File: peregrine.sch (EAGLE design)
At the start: 67 parts, among them IC2 LMV358IDGKR, J1 USB MICRO, U1 ITG-3200, U2 ADXL345, U4 3.3V, U5 ATMEGA32U4-XUAU, Y1 16MHz KX-7

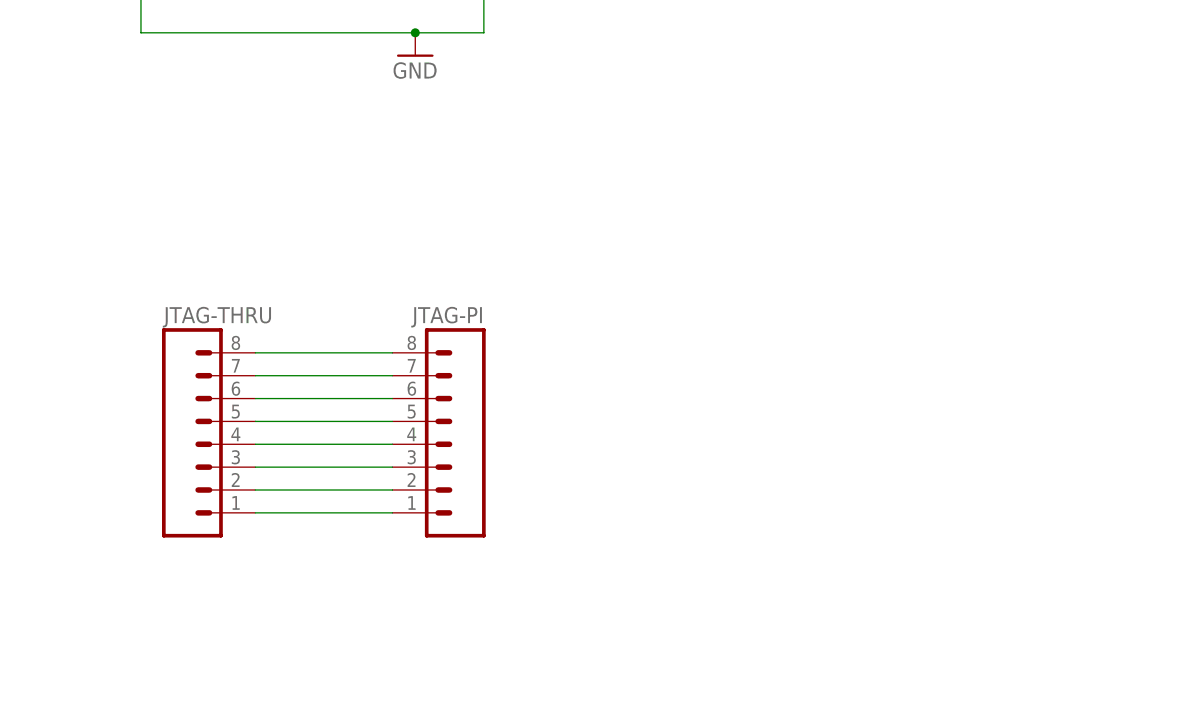
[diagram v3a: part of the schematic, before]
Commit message: Added outline and Pi GPIO, crappy placement
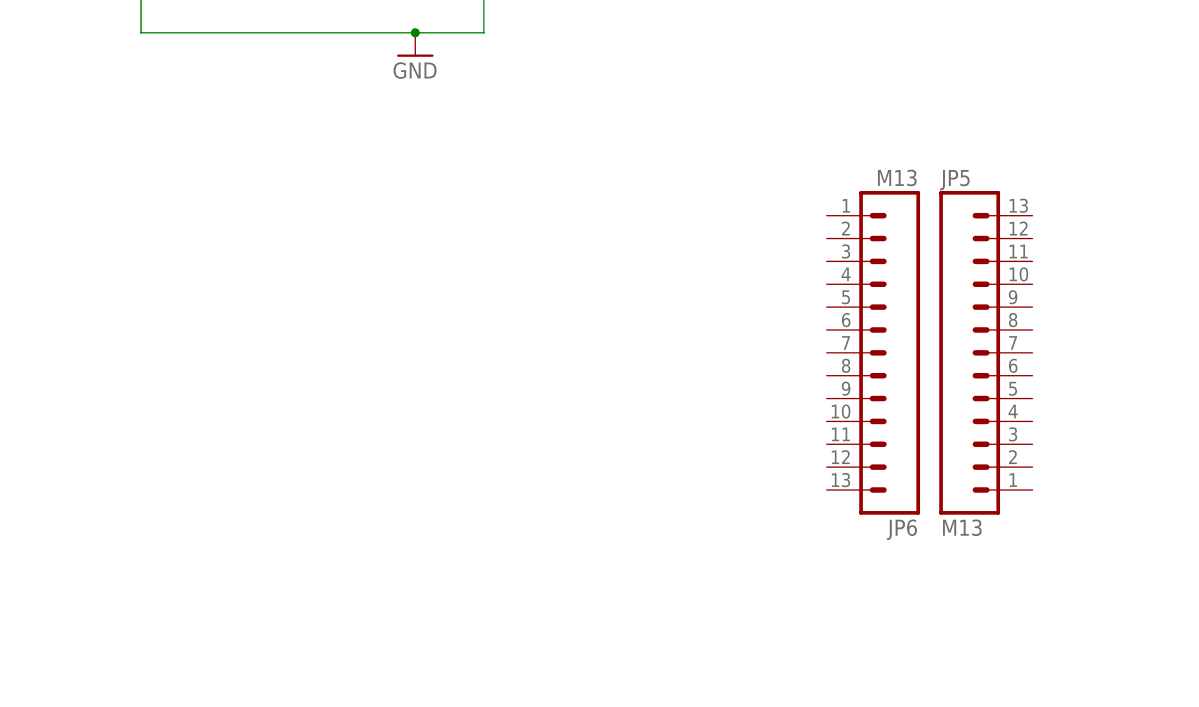
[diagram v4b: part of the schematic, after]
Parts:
- removed JTAG-PI: (no value), SparkFun:M083.5MM-8
- removed JTAG-THRU: (no value), SparkFun:M081X08
- added JP5, JP6: M13, SparkFun:M13
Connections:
- removed net N$14: JTAG-PI.7, JTAG-THRU.7
- removed net N$17: JTAG-PI.6, JTAG-THRU.6
- removed net N$18: JTAG-PI.5, JTAG-THRU.5
- removed net N$19: JTAG-PI.4, JTAG-THRU.4
- removed net N$20: JTAG-PI.3, JTAG-THRU.3
- removed net N$21: JTAG-PI.2, JTAG-THRU.2
- removed net N$22: JTAG-PI.1, JTAG-THRU.1
- removed net N$6: JTAG-PI.8, JTAG-THRU.8
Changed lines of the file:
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@@
 <part name="C14" library="SparkFun" deviceset="CAP" device="0402-CAP" value="0.1uF"/>
 <part name="GND16" library="SparkFun" deviceset="GND" device=""/>
-<part name="JTAG-THRU" library="SparkFun" deviceset="M08" device="1X08"/>
-<part name="JTAG-PI" library="SparkFun" deviceset="M08" device="3.5MM-8"/>
+<part name="JP5" library="SparkFun" deviceset="M13" device=""/>
+<part name="JP6" library="SparkFun" deviceset="M13" device=""/>
 </parts>
 <sheets>
@@
 </instance>
 <instance part="GND16" gate="1" x="-17.78" y="-33.02"/>
-<instance part="JTAG-THRU" gate="G$1" x="104.14" y="106.68"/>
-<instance part="JTAG-PI" gate="G$1" x="129.54" y="106.68" rot="MR0"/>
+<instance part="JP5" gate="G$1" x="185.42" y="116.84"/>
+<instance part="JP6" gate="G$1" x="182.88" y="116.84" rot="R180"/>
 </instances>
 <busses>
@@
 </segment>
 </net>
-<net name="N$6" class="0">
-<segment>
-<pinref part="JTAG-THRU" gate="G$1" pin="8"/>
-<pinref part="JTAG-PI" gate="G$1" pin="8"/>
-<wire x1="109.22" y1="116.84" x2="124.46" y2="116.84" width="0.1524" layer="91"/>
-</segment>
-</net>
-<net name="N$14" class="0">
-<segment>
-<pinref part="JTAG-THRU" gate="G$1" pin="7"/>
-<pinref part="JTAG-PI" gate="G$1" pin="7"/>
-<wire x1="109.22" y1="114.3" x2="124.46" y2="114.3" width="0.1524" layer="91"/>
-</segment>
-</net>
-<net name="N$17" class="0">
-<segment>
-<pinref part="JTAG-THRU" gate="G$1" pin="6"/>
-<pinref part="JTAG-PI" gate="G$1" pin="6"/>
-<wire x1="109.22" y1="111.76" x2="124.46" y2="111.76" width="0.1524" layer="91"/>
-</segment>
-</net>
-<net name="N$18" class="0">
-<segment>
-<pinref part="JTAG-THRU" gate="G$1" pin="5"/>
-<pinref part="JTAG-PI" gate="G$1" pin="5"/>
-<wire x1="109.22" y1="109.22" x2="124.46" y2="109.22" width="0.1524" layer="91"/>
-</segment>
-</net>
-<net name="N$19" class="0">
-<segment>
-<pinref part="JTAG-THRU" gate="G$1" pin="4"/>
-<pinref part="JTAG-PI" gate="G$1" pin="4"/>
-<wire x1="109.22" y1="106.68" x2="124.46" y2="106.68" width="0.1524" layer="91"/>
-</segment>
-</net>
-<net name="N$20" class="0">
-<segment>
-<pinref part="JTAG-THRU" gate="G$1" pin="3"/>
-<pinref part="JTAG-PI" gate="G$1" pin="3"/>
-<wire x1="109.22" y1="104.14" x2="124.46" y2="104.14" width="0.1524" layer="91"/>
-</segment>
-</net>
-<net name="N$21" class="0">
-<segment>
-<pinref part="JTAG-THRU" gate="G$1" pin="2"/>
-<pinref part="JTAG-PI" gate="G$1" pin="2"/>
-<wire x1="109.22" y1="101.6" x2="124.46" y2="101.6" width="0.1524" layer="91"/>
-</segment>
-</net>
-<net name="N$22" class="0">
-<segment>
-<pinref part="JTAG-THRU" gate="G$1" pin="1"/>
-<pinref part="JTAG-PI" gate="G$1" pin="1"/>
-<wire x1="109.22" y1="99.06" x2="124.46" y2="99.06" width="0.1524" layer="91"/>
-</segment>
-</net>

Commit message: Schematic Changes
Changed a number of nets to reflect desired configuration. Added solder
jumpers for potential "serial dyslexia" resloution. Still needs quite a
few net changes to be completely accurate.
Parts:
- removed JP5, JP6: M13, SparkFun:M13
- added BOTTOM, TOP: M13, SparkFun:M13
- added JTAG_THRU: (no value), SparkFun:M081X08
- added SJ1, SJ2, SJ3, SJ4, SJ5, SJ6: (no value), jumper:SJ
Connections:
- removed net COM: GPS.GND, REC_POWER.1
- removed net D2/SDA: U5.(SDA/INT1)PD1
- removed net D3/SCL: U5.(OC0B/SCL/INT0)PD0
- removed net VCC: C11.1, JP3.4, U4.EN, U4.IN
- new net GPIO0(SDA): BOTTOM.2, SJ5.1
- new net GPIO1(SCL): BOTTOM.3, SJ6.1
- new net GPIO10(MOSI): BOTTOM.10
- new net GPIO14(TXD): SJ3.1, TOP.4
- new net GPIO15(RXD): SJ4.1, TOP.5
- new net GPIO17: BOTTOM.6
- new net GPIO18(PCM_CLK): TOP.6
- new net GPIO21(PCM_DOUT): BOTTOM.7
- new net GPIO22: BOTTOM.8
- new net GPIO23: TOP.8
- new net GPIO24: TOP.9
- new net GPIO25: TOP.11
- new net GPIO4(GPCLK0): BOTTOM.4
- new net GPIO7(CE1): TOP.13
- new net GPIO8(CE0): TOP.12
- new net GPIO9(MISO): BOTTOM.11
- new net GPRIO11(SCKL): BOTTOM.12
- new net PI_3V3_1: BOTTOM.1
- new net PI_3V3_2: BOTTOM.9
- new net PI_5V: TOP.1
- new net PI_5V_2: TOP.2
- new net PI_GND1: BOTTOM.5
- new net PI_GND2: BOTTOM.13
- new net PI_GND3: TOP.3
- new net PI_GND4: TOP.7
- new net PI_GND5: TOP.10
- net +5V: now also C11.1, JP3.4, U4.EN, U4.IN
- net D0/RX: now also SJ2.2, SJ3.2
- net D1/TX: now also SJ1.2, SJ4.2
- net GND: now also GPS.GND, REC_POWER.1
- net GPS-RX: now also SJ2.1
- net GPS-TX: now also SJ1.1
- net SCL: now also SJ6.2, U5.(OC0B/SCL/INT0)PD0
- net SDA: now also SJ5.2, U5.(SDA/INT1)PD1
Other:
- note added: "Other"
- note added: "PI-Header"
- note added: "PWM-Related"
- moved on the sheet: C10, C11, C12, C13, C14, C21, C23, C24, C25, C26, C27, C28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

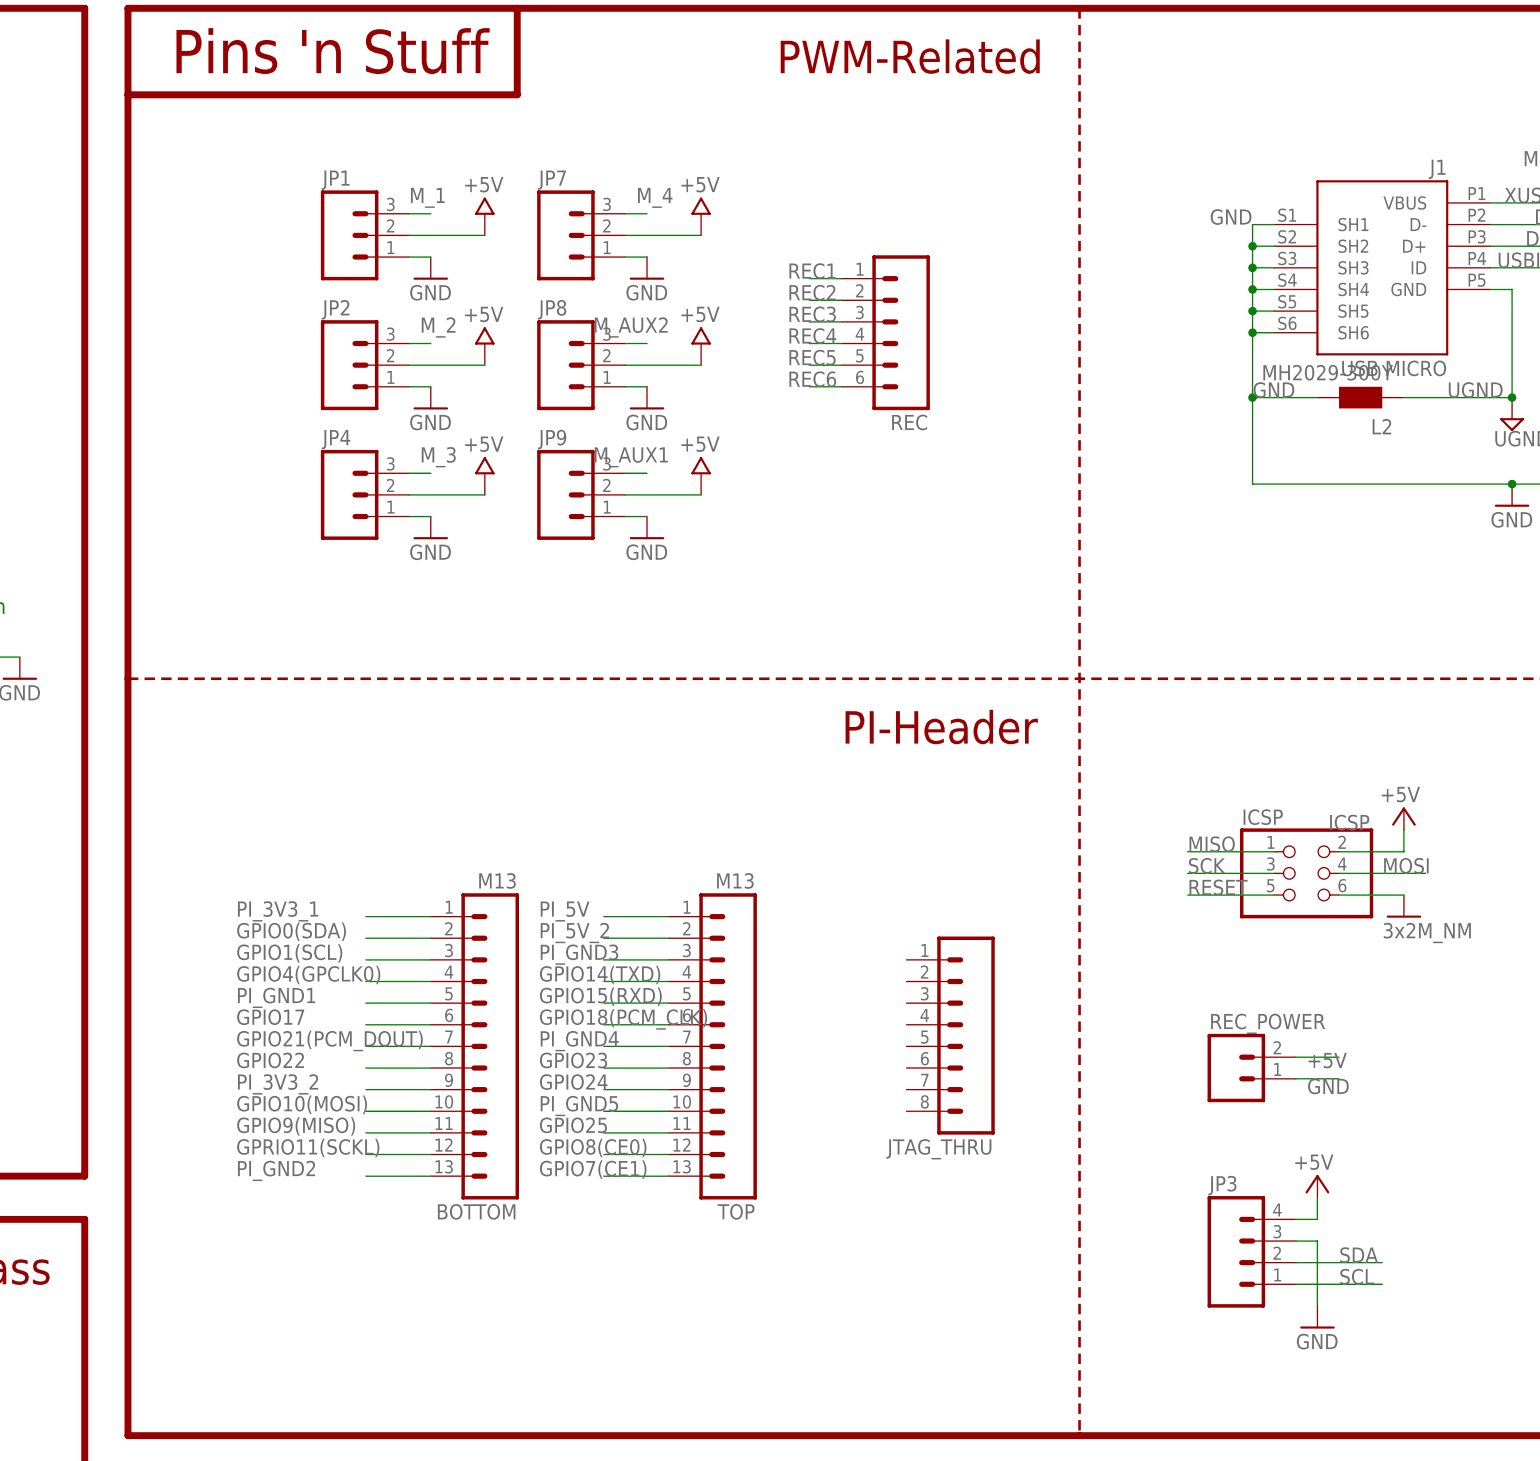
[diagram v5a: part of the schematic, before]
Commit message: Changed around layout.
Changed a bunch of headers so that they were small perofile or locking.
Ignored RCA plug, just assuming that we can build above it. Added two
standoff holes for support above the board. The standoffs would touch on
blank spots on the pi.
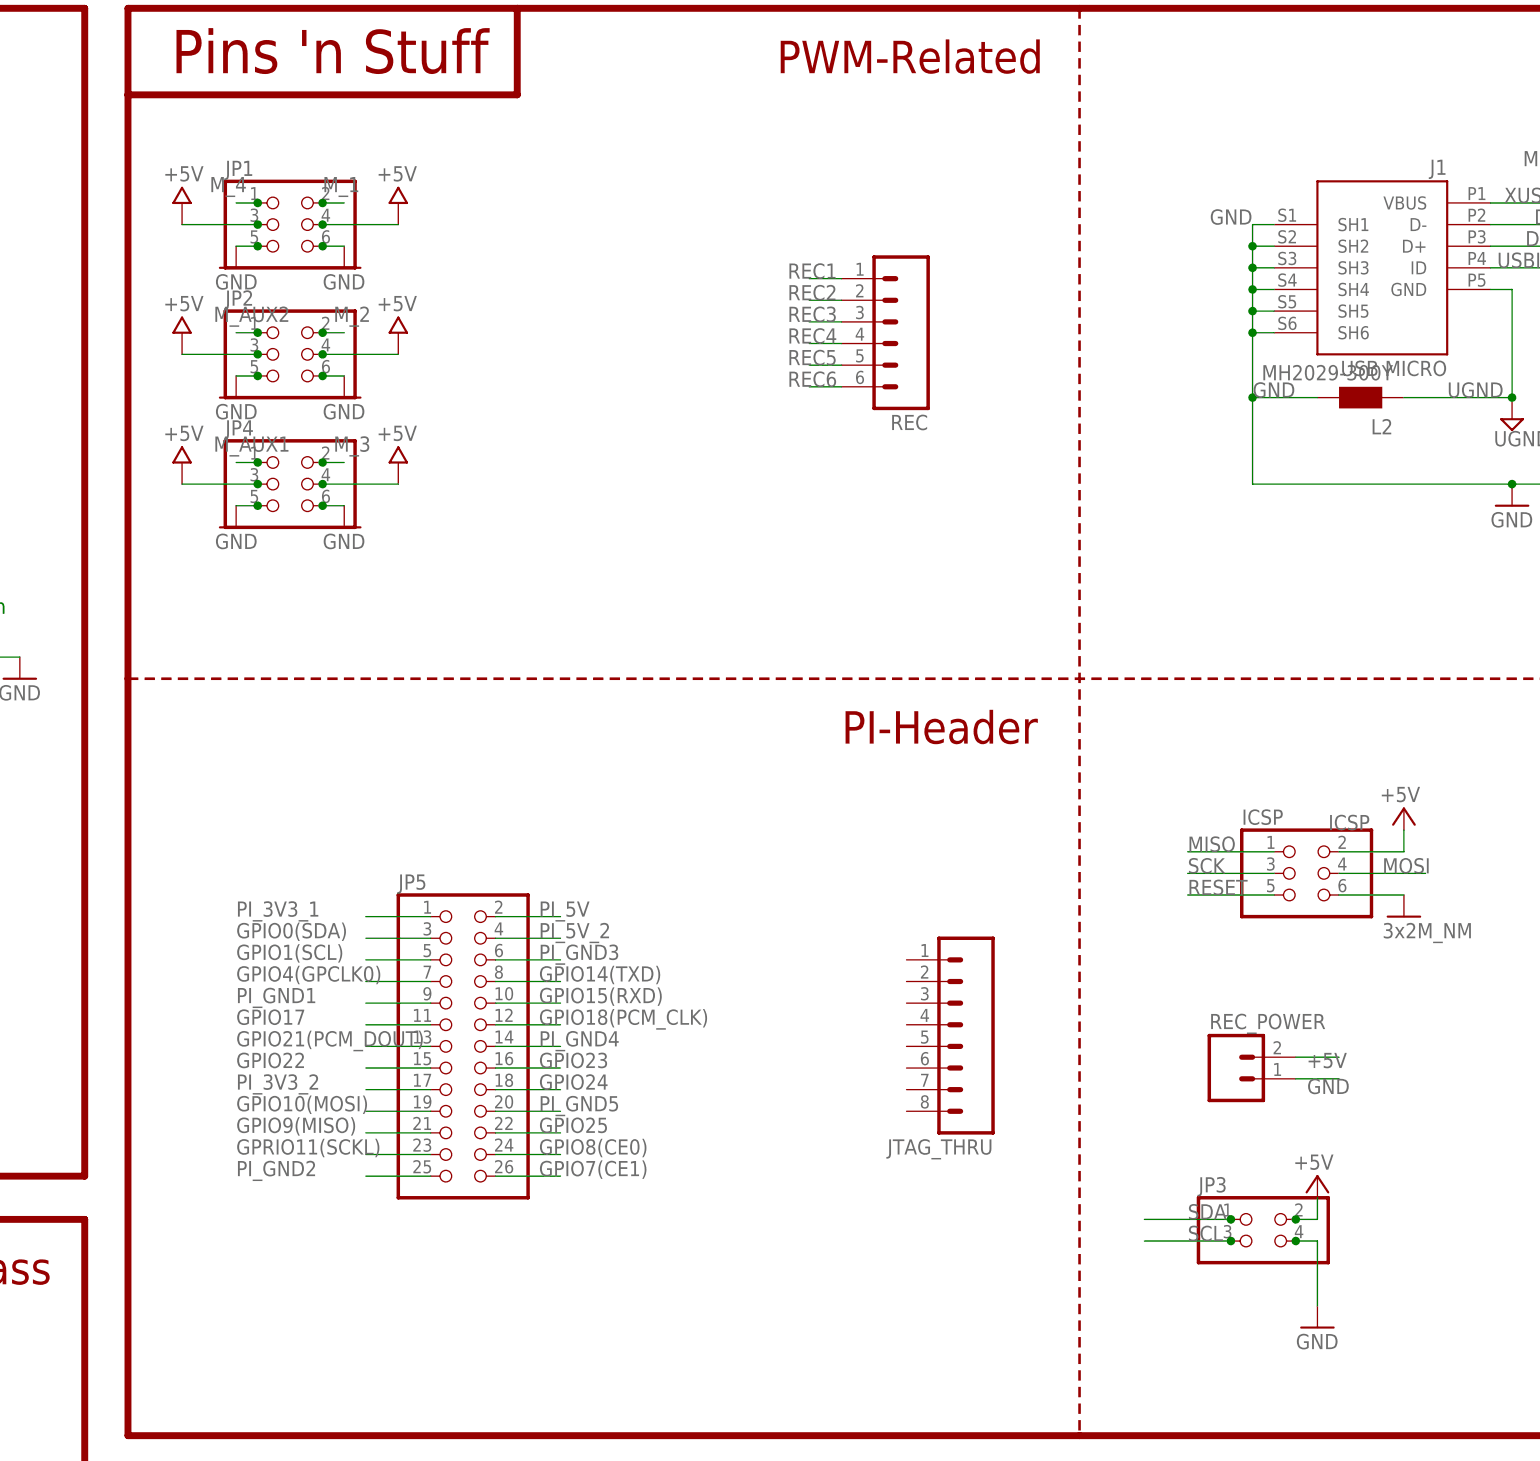
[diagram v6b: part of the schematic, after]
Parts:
- removed BOTTOM, TOP: M13, SparkFun:M13
- removed JP7, JP8, JP9: (no value), SparkFun:M03PTH
- added JP5: (no value), pinhead:PINHD-2X13
- JP1, JP2, JP4: device SparkFun:M03PTH -> pinhead:PINHD-2X3
- JP3: device SparkFun:M04PTH -> pinhead:PINHD-2X2
- JTAG_THRU: device SparkFun:M081X08 -> SparkFun:M08LOCK
- REC: device SparkFun:M06SIP -> SparkFun:M06LOCK
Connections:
- removed net GPIO18(PCM_CLK): TOP.6
- removed net GPIO23: TOP.8
- removed net GPIO24: TOP.9
- removed net GPIO25: TOP.11
- removed net GPIO7(CE1): TOP.13
- removed net GPIO8(CE0): TOP.12
- removed net PI_5V: TOP.1
- removed net PI_5V_2: TOP.2
- removed net PI_GND3: TOP.3
- removed net PI_GND4: TOP.7
- removed net PI_GND5: TOP.10
- net +5V: now also JP1.3, JP1.4, JP2.3, JP2.4, JP3.2, JP4.3, JP4.4; no longer JP1.2, JP2.2, JP3.4, JP4.2, JP7.2, JP8.2, JP9.2
- net GND: now also JP1.5, JP1.6, JP2.5, JP2.6, JP3.4, JP4.5, JP4.6; no longer JP1.1, JP2.1, JP3.3, JP4.1, JP7.1, JP8.1, JP9.1
- net GPIO0(SDA): now also JP5.3; no longer BOTTOM.2
- net GPIO1(SCL): now also JP5.5; no longer BOTTOM.3
- net GPIO10(MOSI): now also JP5.19; no longer BOTTOM.10
- net GPIO14(TXD): no longer TOP.4
- net GPIO15(RXD): no longer TOP.5
- net GPIO17: now also JP5.11; no longer BOTTOM.6
- net GPIO21(PCM_DOUT): now also JP5.13; no longer BOTTOM.7
- net GPIO22: now also JP5.15; no longer BOTTOM.8
- net GPIO4(GPCLK0): now also JP5.7; no longer BOTTOM.4
- net GPIO9(MISO): now also JP5.21; no longer BOTTOM.11
- net GPRIO11(SCKL): now also JP5.23; no longer BOTTOM.12
- net M_1: now also JP1.2; no longer JP1.3
- net M_2: now also JP2.2; no longer JP2.3
- net M_3: now also JP4.2; no longer JP4.3
- net M_4: now also JP1.1; no longer JP7.3
- net M_AUX1: now also JP4.1; no longer JP9.3
- net M_AUX2: now also JP2.1; no longer JP8.3
- net PI_3V3_1: now also JP5.1; no longer BOTTOM.1
- net PI_3V3_2: now also JP5.17; no longer BOTTOM.9
- net PI_GND1: now also JP5.9; no longer BOTTOM.5
- net PI_GND2: now also JP5.25; no longer BOTTOM.13
- net SCL: now also JP3.3; no longer JP3.1
- net SDA: now also JP3.1; no longer JP3.2
